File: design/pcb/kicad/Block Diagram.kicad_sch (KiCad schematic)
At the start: 0 parts

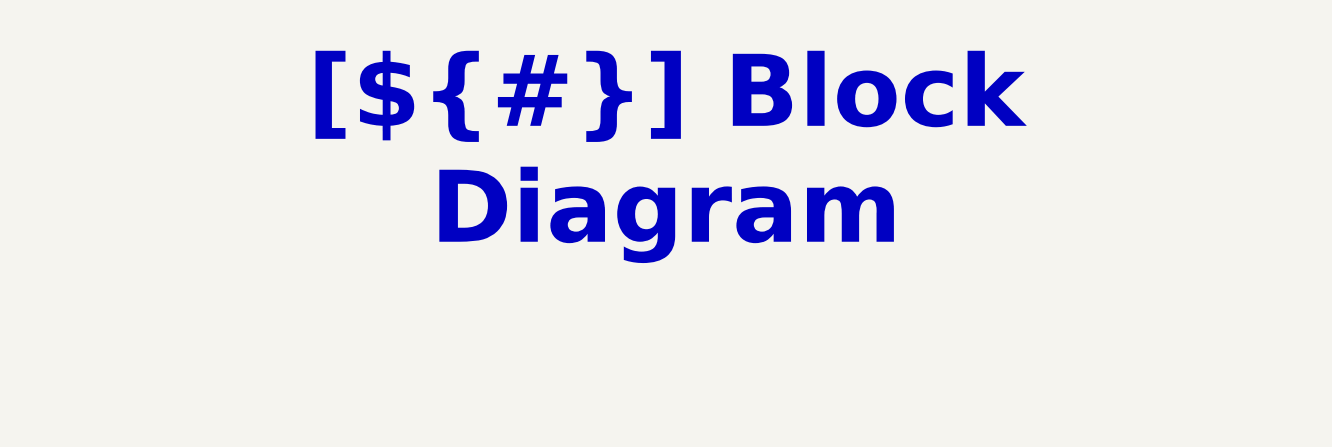
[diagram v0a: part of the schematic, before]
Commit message: Add LCD and STLink schematic sheets, update KiCad project files
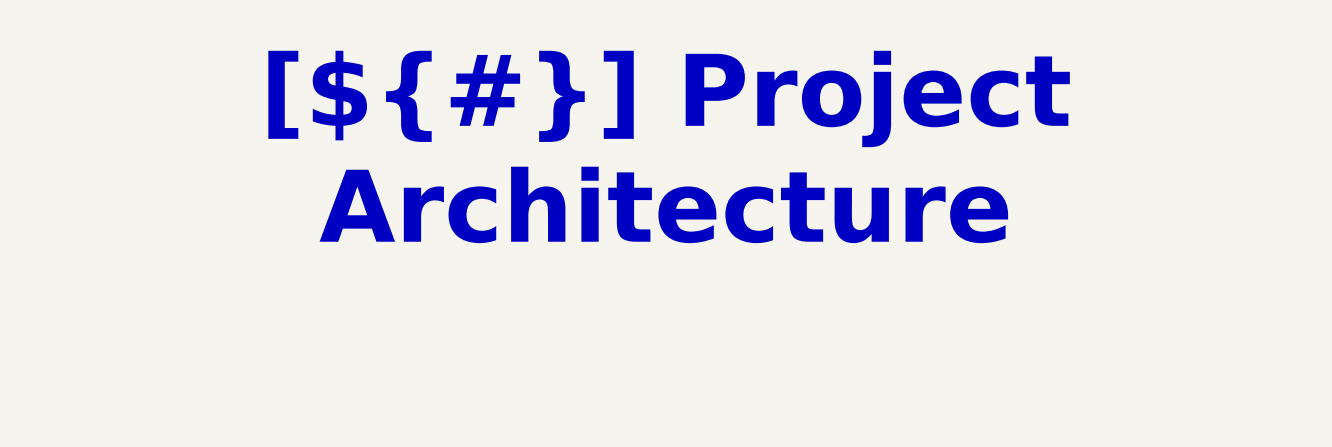
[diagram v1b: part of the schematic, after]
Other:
- title: Block Diagram -> Project Architecture
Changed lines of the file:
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@@
 	(paper "A3")
 	(title_block
-		(title "Block Diagram")
+		(title "Project Architecture")
 		(date "2025-01-12")
 		(rev "${REVISION}")
